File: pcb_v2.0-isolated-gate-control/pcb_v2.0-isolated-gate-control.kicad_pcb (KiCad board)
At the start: 4 copper layers, 170 x 110 mm, 167 parts, among them J1 ServoLock, J10 Buttons, J11 2x encoder, J12 limit-g2, J13 Relay VFD2 [NO, COM, NC], J14 GND-P, J15 OD, J16 Power-LightBarrier-12V, J17 3V3 5V VDD, J18 GNDD, J19 OD, J2 supply, J20 OD, J21 limit-g1, J3 12V-filtered, J4 light-barrier, reserve, J5 GND-P, J6 2x remoteControl, J7 Relay VFD1 [NO, COM, NC], J8 RS485, K1 RT314A24, K2 RT314A24, Q1 2N7000, Q2 2N7000, Q3 IRF5305, Q6 IRF5305, U1 esp32-devkit-v1_30Pin, U4 MAX485E, U5 L78S05CV_TO220, U6 ULN2803A

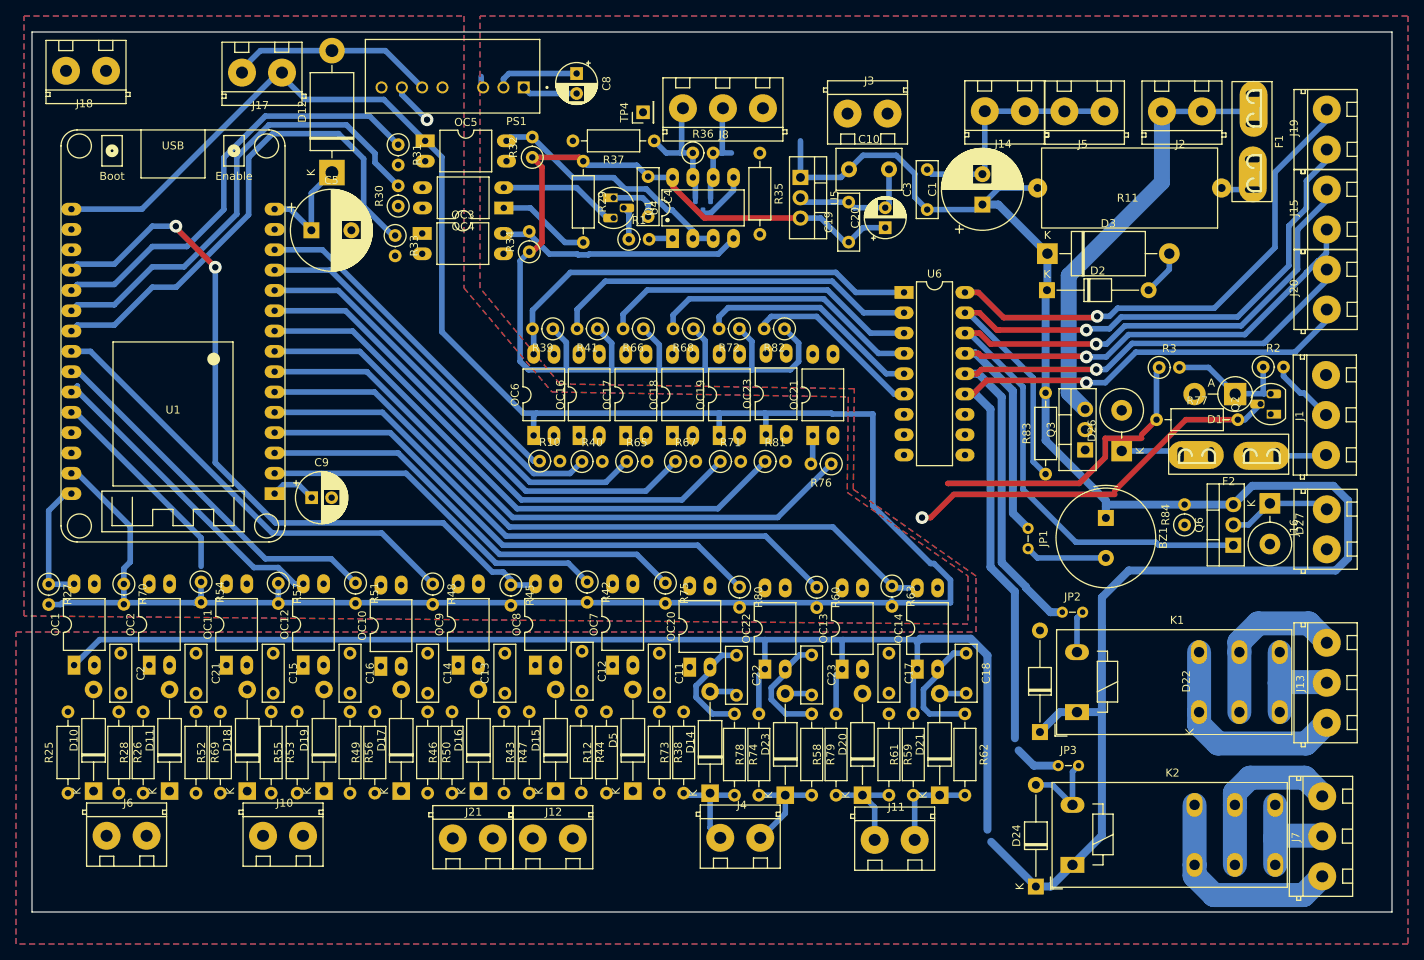
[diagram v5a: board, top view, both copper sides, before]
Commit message: pcb: routing complete (DRC pass)
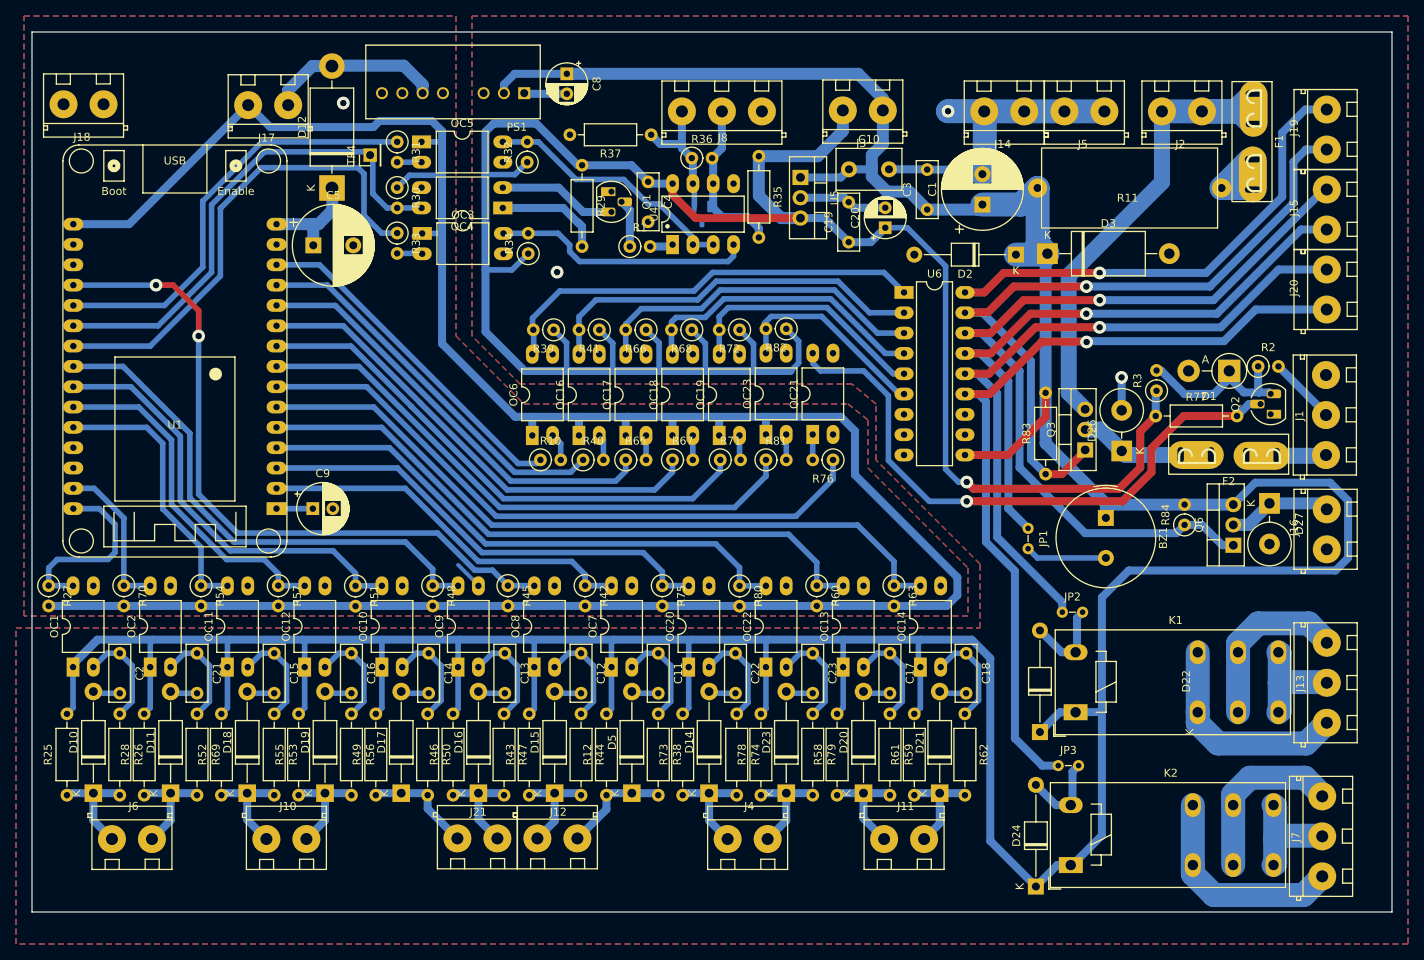
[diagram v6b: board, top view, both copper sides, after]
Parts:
- moved TP4 34.5 mm to (77.3, 40.4)
- moved D2 5.90 mm to (158.0, 52.8), turned to 180 degrees
- moved C13 5.00 mm to (94.1, 102.7), turned to -90 degrees
- moved J3 4.43 mm to (141.4, 34.8), turned to 180 degrees
- moved J18 4.20 mm to (43.9, 34.0)
- moved J17 4.14 mm to (67.0, 34.1)
- moved D1 2.99 mm to (184.7, 67.4)
- moved R3 2.94 mm to (175.6, 69.8), turned to 90 degrees
- moved R30 2.32 mm to (80.6, 44.5), turned to -90 degrees
- moved D12 1.93 mm to (72.5, 44.5)
- moved C5 1.89 mm to (70.2, 51.7)
- moved U1 1.89 mm to (52.9, 84.6)
- moved C9 1.38 mm to (70.1, 84.6)
- moved C8 1.22 mm to (101.9, 30.2)
- moved J11 1.18 mm to (141.5, 125.9)
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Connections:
- J3 pad 2: +12V -> +5VA
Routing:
- net +12V: track 394.8 -> 546.0 mm
- net +5VA: track 184.8 -> 268.5 mm, vias 0 -> 1
- net Net-(Q2-G): track 48.0 -> 75.9 mm
- net GNDPWR: track 81.8 -> 101.0 mm, vias 0 -> 3
- net /isolated-digital-input_sw-to-gnd3/in_switchToGND: track 0.00 -> 13.6 mm
- net /isolated-digital-input_sw-to-gnd/in_switchToGND: track 0.00 -> 13.6 mm
- net /isolated-digital-input_sw-to-gnd4/in_switchToGND: track 0.00 -> 13.5 mm
- net /isolated-digital-input_sw-to-gnd5/in_switchToGND: track 0.00 -> 13.5 mm
- net /isolated-digital-input_sw-to-gnd9/in_switchToGND: track 0.00 -> 13.5 mm
- net /isolated-digital-input_sw-to-gnd8/in_switchToGND: track 0.00 -> 13.5 mm
- net /isolated-digital-input_sw-to-gnd1/in_switchToGND: track 0.00 -> 13.2 mm
- net /isolated-digital-input_sw-to-gnd2/in_switchToGND: track 0.00 -> 13.2 mm
- net Net-(C14-Pad1): track 0.00 -> 12.9 mm
- net Net-(C13-Pad1): track 0.00 -> 12.9 mm
- net Net-(C15-Pad1): track 0.00 -> 12.9 mm
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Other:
- board text added: "12V filtered"
- board text added: "12V supply"
- board text added: "GND A B RS485"
- board text added: "GND GND"

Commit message: pcb: Add text, testpoints, mounting-holes
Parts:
- removed U1: esp32-devkit-v1_30Pin, devboards_libJonny:esp32-devkit-v1_30Pin
- added H1: MountingHole_Pad, mountingHoles_libJonny:MountingHole_2.2mm_NPTH-with-pad_DRC-clearance-error, F.Cu at (38.5, 43.5)
- added H10: MountingHole_Pad, mountingHoles_libJonny:MountingHole_2.2mm_NPTH-with-pad_DRC-clearance-error, F.Cu at (167.5, 43.0)
- added H11: MountingHole_Pad, mountingHoles_libJonny:MountingHole_2.2mm_NPTH-with-pad_DRC-clearance-error, F.Cu at (201.5, 64.0)
- added H12: MountingHole_Pad, mountingHoles_libJonny:MountingHole_2.2mm_NPTH-with-pad_DRC-clearance-error, F.Cu at (140.8, 54.0)
- added H13: MountingHole_Pad, mountingHoles_libJonny:MountingHole_2.2mm_NPTH-with-pad_DRC-clearance-error, F.Cu at (81.5, 58.0)
- added H14: MountingHole_Pad, mountingHoles_libJonny:MountingHole_2.2mm_NPTH-with-pad_DRC-clearance-error, F.Cu at (79.7, 85.1)
- added H2: MountingHole_Pad, mountingHoles_libJonny:MountingHole_2.2mm_NPTH-with-pad_DRC-clearance-error, F.Cu at (37.8, 88.5)
- added H3: MountingHole_Pad, mountingHoles_libJonny:MountingHole_2.2mm_NPTH-with-pad_DRC-clearance-error, F.Cu at (136.5, 89.0)
- added H4: MountingHole_Pad, mountingHoles_libJonny:MountingHole_2.2mm_NPTH-with-pad_DRC-clearance-error, F.Cu at (107.2, 28.5)
- added H5: MountingHole_Pad, mountingHoles_libJonny:MountingHole_2.2mm_NPTH-with-pad_DRC-clearance-error, F.Cu at (172.5, 116.0)
- added H6: MountingHole_Pad, mountingHoles_libJonny:MountingHole_2.2mm_NPTH-with-pad_DRC-clearance-error, F.Cu at (201.5, 28.5)
- added H7: MountingHole_Pad, mountingHoles_libJonny:MountingHole_2.2mm_NPTH-with-pad_DRC-clearance-error, F.Cu at (39.0, 126.0)
- added H8: MountingHole_Pad, mountingHoles_libJonny:MountingHole_2.2mm_NPTH-with-pad_DRC-clearance-error, F.Cu at (79.0, 126.0)
- added H9: MountingHole_Pad, mountingHoles_libJonny:MountingHole_2.2mm_NPTH-with-pad_DRC-clearance-error, F.Cu at (134.0, 126.0)
- added J9: Conn_01x03_Pin, Connector_PinHeader_2.54mm:PinHeader_1x03_P2.54mm_Vertical, F.Cu at (50.6, 31.9)
- added TP1: TP DIR, Connector_PinHeader_2.54mm:PinHeader_1x01_P2.54mm_Vertical, F.Cu at (54.7, 36.6)
- added TP10: GND, Connector_PinHeader_2.54mm:PinHeader_1x01_P2.54mm_Vertical, F.Cu at (75.5, 84.8)
- added TP11: GNDPWR, Connector_PinHeader_2.54mm:PinHeader_1x01_P2.54mm_Vertical, F.Cu at (168.4, 67.2)
- added TP12: TP-servoPWM, Connector_PinHeader_2.54mm:PinHeader_1x01_P2.54mm_Vertical, F.Cu at (189.6, 63.0)
- added TP2: TP TX, Connector_PinHeader_2.54mm:PinHeader_1x01_P2.54mm_Vertical, F.Cu at (77.2, 44.4)
- added TP3: TP A, Connector_PinHeader_2.54mm:PinHeader_1x01_P2.54mm_Vertical, F.Cu at (130.7, 34.1)
- added TP5: TP B, Connector_PinHeader_2.54mm:PinHeader_1x01_P2.54mm_Vertical, F.Cu at (111.8, 34.2)
- added TP6: 12V, Connector_PinHeader_2.54mm:PinHeader_1x01_P2.54mm_Vertical, F.Cu at (145.7, 31.8)
- added TP7: 5V, Connector_PinHeader_2.54mm:PinHeader_1x01_P2.54mm_Vertical, F.Cu at (131.1, 52.8)
- added TP8: GNDPWR, Connector_PinHeader_2.54mm:PinHeader_1x01_P2.54mm_Vertical, F.Cu at (149.7, 31.8)
- added TP9: Vin, Connector_PinHeader_2.54mm:PinHeader_1x01_P2.54mm_Vertical, F.Cu at (180.5, 51.6)
- added U2: esp32-devkit-v1_30Pin, devboards_libJonny:esp32-devkit-v1_30Pin, F.Cu at (52.8, 84.6)
- D1: value TVS 12V -> TVS 5V
- J3: value 12V-filtered -> 12V 5V
- TP4: value TP UART RX -> RX
- moved C9 1.10 mm to (69.0, 84.6)
- moved Q1 1.02 mm to (107.4, 46.0)
- moved D22 0.51 mm to (160.5, 112.5)
- moved K1 0.51 mm to (164.9, 110.0)
- moved J13 0.51 mm to (196.3, 111.3)
- moved JP2 0.51 mm to (163.3, 97.5)
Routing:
- net GNDPWR: track 101.0 -> 124.2 mm, vias 3 -> 6
- net GND: track 3.66 -> 26.6 mm, vias 1 -> 5
- net +5V: track 22.0 -> 35.4 mm
- net RS485_A: track 20.5 -> 31.9 mm
- net +BATT: track 66.2 -> 75.3 mm
- net /RS485-UART_DIR-T: track 53.8 -> 61.7 mm
- net +12V: track 546.0 -> 553.7 mm
- net +3V3: track 302.6 -> 308.5 mm
- net RS485_B: track 16.9 -> 21.6 mm
- net +5VA: track 268.5 -> 273.0 mm
- net /Servo-PWM-Signal: track 8.54 -> 12.8 mm
- net /dIn_Encoder2: track 91.5 -> 94.0 mm
- net /dIn_RemoteOpen: track 23.9 -> 22.8 mm
- net Net-(U2-EN): track 4.54 -> 3.43 mm
- net Net-(Q1-G): track 6.01 -> 5.00 mm
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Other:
- board text added: "5V 3V3 GND"
- board text added: "<="
- board text added: "A"
- board text added: "All Isolated: - 5V, 3V3 - RS485 - 12x digital-in - 6x open drain - 2x relay - 2x 12V (P-MOS) - Buzzer - PWM (Servo signal)"
- board text added: "Antenna"
- board text added: "B"
- board text added: "Buttons OPEN, CLOSE"
- board text added: "Digital Inputs"
- board text added: "ESP32-DevKit-V1 (30pin)"
- board text added: "Encoder 1 2"
- board text added: "Fuse-PCB"
- board text added: "GND"
- board text added: "GND 12V"
- board text added: "Isolated 3V3 5V"
- board text added: "Isolated GND"
- board text added: "LightBarrier GND 12V"
- board text added: "LightBarrier RESERVE"
- board text added: "Limit switches C1, O1, C2, O2"
- board text added: "Open-Drain outputs VFD1 VFD2 BZ LB SV LED"
- board text added: "RS485 DIR"
- board text added: "RX"
- board text added: "Remote OPEN, CLOSE"
- board text added: "Servo 12V PWM GND"
- board text added: "Servo-PWM"
- board text added: "Supply IN 12V 12V"
- board text added: "Switch to GND non-inverting"
- board text added: "TX"
- board text added: "USB"
- board text added: "V-in"
- board text added: "VFD1 NC NO COM"
- board text added: "pcb_isolated-gate-control Gate V2.0 28.12.2024"
- board text removed: "12V supply"
- board text removed: "F-Control"

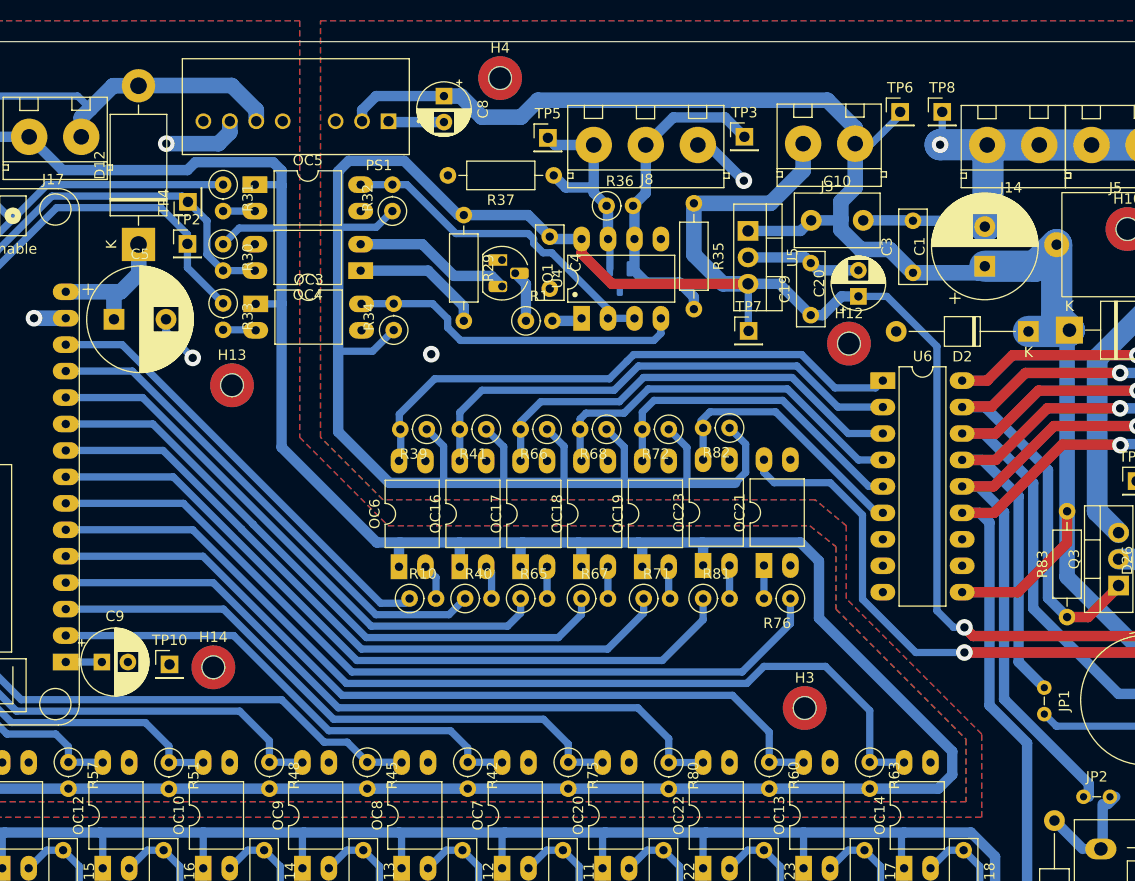
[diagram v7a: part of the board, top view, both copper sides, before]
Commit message: pcb: Add NOT-Gate (optocouplers off in idle), Replace ULN28 with 7Ch
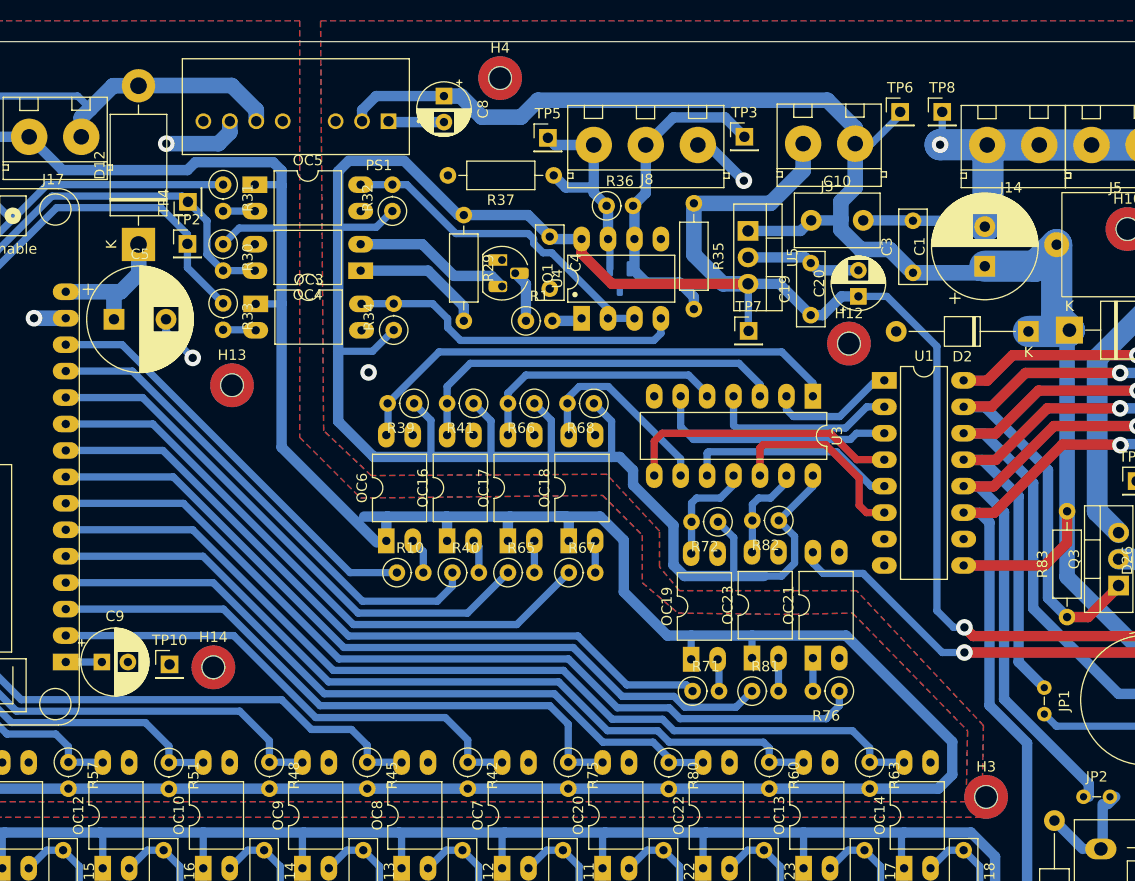
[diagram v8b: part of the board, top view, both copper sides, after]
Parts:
- removed U6: ULN2803A, Package_DIP:DIP-18_W7.62mm_LongPads
- added U1: ULN2003, Package_DIP:DIP-16_W7.62mm_LongPads, F.Cu at (144.1, 57.5)
- added U3: 74HC04, Package_DIP:DIP-14_W7.62mm_LongPads, F.Cu at (137.3, 59.1)
- R82: value 4k7 -> 10k
- moved H3 19.4 mm to (153.9, 97.5)
- moved R72 10.1 mm to (128.2, 71.1)
- moved R82 10.1 mm to (134.0, 71.0)
- moved R76 10.1 mm to (139.8, 87.4)
- moved OC23 10.1 mm to (131.4, 84.2)
- moved R71 10.1 mm to (125.7, 87.4)
- moved R81 10.1 mm to (131.4, 87.4)
- moved OC21 10.1 mm to (137.3, 84.2)
- moved OC19 10.1 mm to (125.6, 84.3)
- moved OC16 2.77 mm to (102.2, 72.9)
- moved OC17 2.77 mm to (108.0, 72.9)
- moved OC18 2.77 mm to (113.8, 72.9)
- moved OC6 2.77 mm to (96.3, 72.9)
- moved R10 2.77 mm to (97.3, 76.0)
- moved R40 2.77 mm to (102.7, 76.0)
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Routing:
- net Net-(U1-I4): track 0.00 -> 26.8 mm
- net Net-(U1-I3): track 0.00 -> 23.2 mm
- net Net-(OC19-Pad4): track 31.7 -> 10.5 mm
- net Net-(U1-I5): track 0.00 -> 20.6 mm
- net Net-(U1-I6): track 0.00 -> 19.0 mm
- net Net-(U1-I2): track 0.00 -> 18.2 mm
- net Net-(OC18-Pad4): track 37.2 -> 19.4 mm
- net Net-(OC17-Pad4): track 42.5 -> 24.9 mm
- net +5VA: track 273.0 -> 289.4 mm
- net Net-(OC23-Pad4): track 24.9 -> 9.40 mm
- net Net-(Q2-G): track 75.9 -> 62.7 mm
- net Net-(U1-I1): track 0.00 -> 12.4 mm
- net Net-(OC16-Pad4): track 48.8 -> 37.6 mm
- net Net-(OC6-Pad4): track 54.4 -> 48.5 mm
- net /dOut_ServoPWM: track 80.6 -> 84.7 mm
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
